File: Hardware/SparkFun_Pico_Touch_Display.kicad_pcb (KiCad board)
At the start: 4 copper layers, 58.4 x 50.8 mm, 89 parts, among them J1 Conn_01x20, J2 Conn_01x20, J3 Conn_02x10_SMD_RA, J4 Conn_1x21_FPC, J5 Qwiic_Vertical, J6 microSD, Q1 RE1C002UNTCL, SW1 SMD_4.6x2.8mm_h2.5mm, U1 2" LCD-TFT 240x320, U2 PCA9554PW

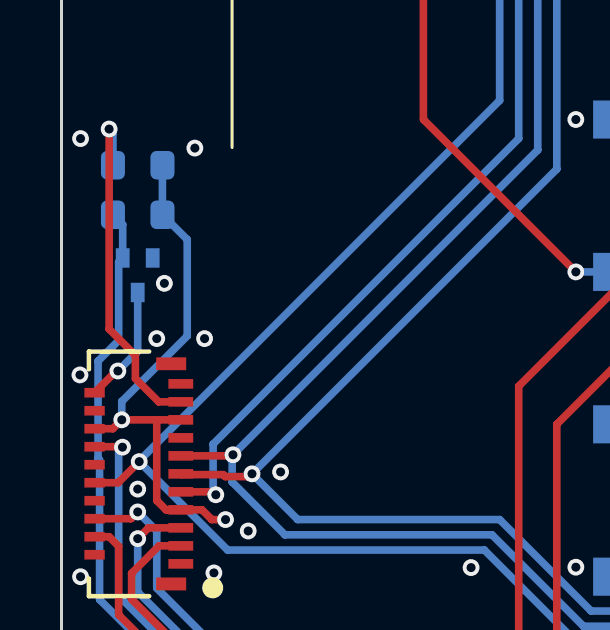
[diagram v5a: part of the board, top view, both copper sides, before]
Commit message: Review updates
Add 2x20 connector PROD_ID
Move R6
Swap In1.Cu and In2.Cu
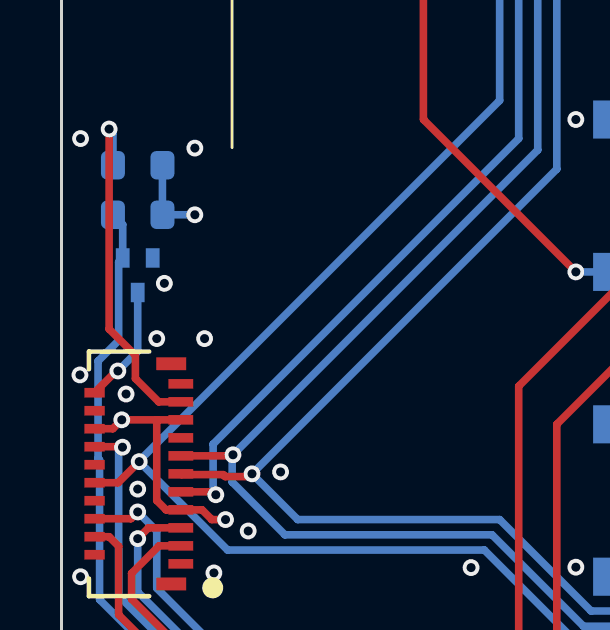
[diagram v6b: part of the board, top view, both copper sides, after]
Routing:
- net 3.3V: track 49.2 -> 42.2 mm, vias 11 -> 12
- net GND: vias 93 -> 94
- added copper zone on In1.Cu, net 3.3V
- added copper zone on In2.Cu, net GND
- removed copper zone on In2.Cu, net 3.3V
- removed copper zone on In1.Cu, net GND
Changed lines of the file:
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@@
 		(tags "SparkFun resistor")
 		(property "Reference" "R6"
-			(at 0 1.43 360)
+			(at 0 1.43 0)
 			(layer "B.Fab")
 			(effects
@@
 		)
 		(property "Value" "100k"
-			(at 0 -1.43 360)
+			(at 0 -1.43 0)
 			(layer "B.Fab")
 			(effects
@@
 	)
 	(via
+		(at 120.015 95.885)
+		(size 0.56)
+		(drill 0.3)
+		(layers "F.Cu" "B.Cu")
+		(net 2)
+	)
+	(via
 		(at 135.89 113.03)
 		(size 0.56)
@@
 	)
 	(segment
-		(start 119.761 99.926102)
-		(end 119.761 96.711)
-		(width 0.254)
-		(layer "B.Cu")
-		(net 2)
-	)
-	(segment
-		(start 119.761 96.711)
-		(end 118.935 95.885)
-		(width 0.254)
-		(layer "B.Cu")
-		(net 2)
-	)
-	(segment
-		(start 117.579102 102.720102)
-		(end 117.579102 102.108)
-		(width 0.254)
-		(layer "B.Cu")
-		(net 2)
-	)
-	(segment
-		(start 117.579102 102.108)
-		(end 119.761 99.926102)
-		(width 0.254)
-		(layer "B.Cu")
-		(net 2)
-	)
-	(segment
 		(start 116.7511 119.38)
 		(end 116.7511 116.84)
@@
 	)
 	(segment
+		(start 118.935 95.885)
+		(end 120.015 95.885)
+		(width 0.254)
+		(layer "B.Cu")
+		(net 2)
+	)
+	(segment
 		(start 142.685 115.57)
 		(end 142.685 116.522)
@@
 	)
 	(via
+		(at 117.722733 101.860267)
+		(size 0.56)
+		(drill 0.3)
+		(layers "F.Cu" "B.Cu")
+		(free yes)
+		(net 3)
+	)
+	(via
 		(at 135.89 110.8075)
 		(size 0.56)
@@
 		(net 3)
 		(net_name "GND")
-		(layers "F.Cu" "In1.Cu" "B.Cu")
+		(layers "F.Cu" "In2.Cu" "B.Cu")
 		(hatch edge 0.5)
 		(connect_pads
@@
 		(net 2)
 		(net_name "3.3V")
-		(layer "In2.Cu")
+		(layer "In1.Cu")
 		(hatch edge 0.5)
 		(connect_pads

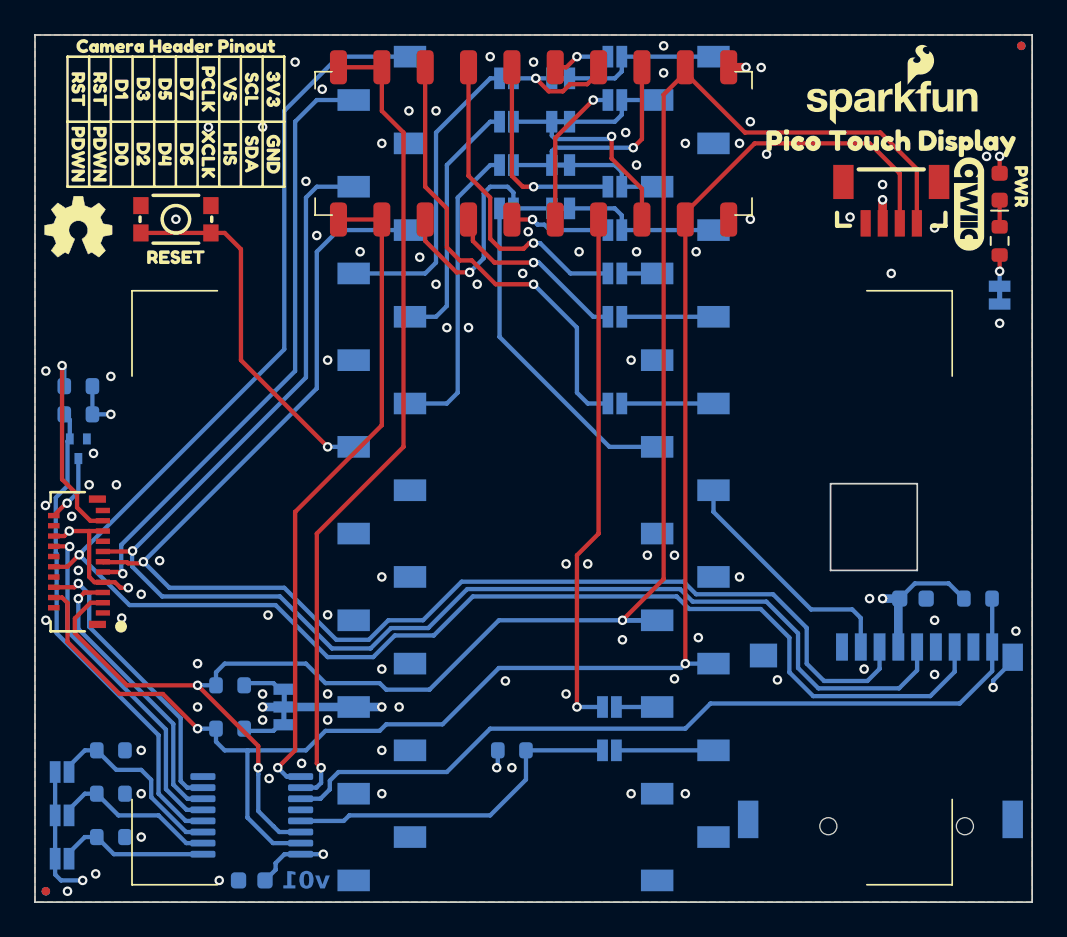
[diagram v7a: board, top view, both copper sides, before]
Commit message: Move display connector to bottom
Previous location was too easy to accidentally unlatch
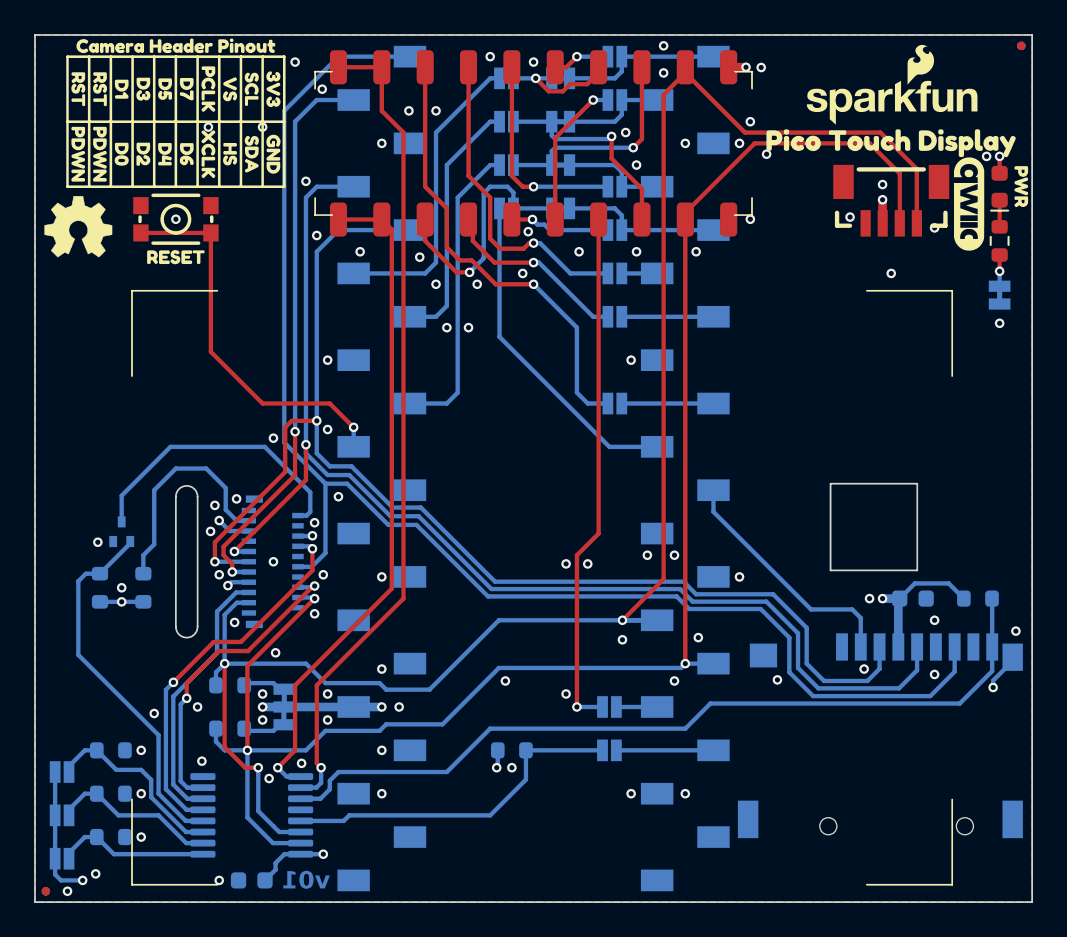
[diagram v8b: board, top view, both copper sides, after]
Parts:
- J4: moved to B.Cu
- moved R1 12.4 mm to (121.9, 106.0), turned to -90 degrees
- moved J4 11.4 mm to (129.5, 104.5)
- moved R2 10.2 mm to (119.4, 106.0), turned to -90 degrees
- moved Q1 4.58 mm to (120.7, 102.2), turned to 180 degrees
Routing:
- net GPIO16/POCI/DC: track 102.9 -> 83.4 mm, vias 1 -> 0
- net GPIO18/SCK: track 86.1 -> 72.0 mm, vias 1 -> 2
- net Net-(J4-Pin_2): track 3.97 -> 16.8 mm, vias 1 -> 0
- net GPIO19/PICO: track 83.0 -> 73.3 mm, vias 1 -> 2
- net SCL/GPIO5: track 108.4 -> 101.6 mm
- net DISP_BL: track 28.5 -> 21.7 mm
- net 3.3V: track 42.2 -> 37.9 mm, vias 12 -> 13
- net GPIO17/DISP_~{CS}: track 35.9 -> 33.3 mm, vias 1 -> 2
- net SDA/GPIO4: track 98.2 -> 95.7 mm, vias 2 -> 3
- net DISP_~{RST}: track 20.3 -> 22.1 mm, vias 1 -> 2
- net Net-(J4-Pin_3): track 11.8 -> 13.2 mm, vias 1 -> 0
- net TP_INT: track 16.9 -> 15.6 mm, vias 1 -> 0
- net TP_~{RESET}: track 17.1 -> 18.2 mm, vias 1 -> 2
- net RUN: track 21.5 -> 22.4 mm
- net GND: vias 94 -> 96
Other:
- outline, holes or cut-outs redrawn
